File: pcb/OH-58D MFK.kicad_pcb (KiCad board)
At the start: 2 copper layers, 114.5 x 140 mm, 123 parts, among them J1 Conn_01x07_Pin, J2 Conn_01x10_Pin, J3 Conn_01x03_Pin, J4 Conn_01x02_Pin, J5 Conn_01x02_Pin, SW1 SW_Push, SW10 SW_Push, SW11 SW_Push, SW12 SW_Push, SW13 SW_Push, SW14 SW_Push, SW15 SW_Push, SW16 SW_Push, SW17 SW_Push, SW18 SW_Push, SW19 SW_Push, SW2 SW_Push, SW20 SW_Push, SW21 SW_Push, SW22 SW_Push, SW23 SW_Push, SW24 SW_Push, SW25 SW_Push, SW26 SW_Push, SW27 SW_Push, SW28 SW_Push, SW29 SW_Push, SW3 SW_Push, SW30 SW_Push, SW31 SW_Push, SW32 SW_Push, SW33 SW_Push, SW34 SW_Push, SW35 SW_Push, SW36 SW_Push, SW37 SW_Push, SW38 SW_Push, SW39 SW_Push, SW4 SW_Push, SW40 SW_Push, SW41 SW_Push, SW42 SW_Push, SW43 SW_Push, SW44 SW_Push, SW45 SW_Push, SW46 SW_Push, SW47 SW_Push, SW5 SW_Push, SW6 SW_Push, SW7 SW_Push, SW8 SW_Push, SW9 SW_Push

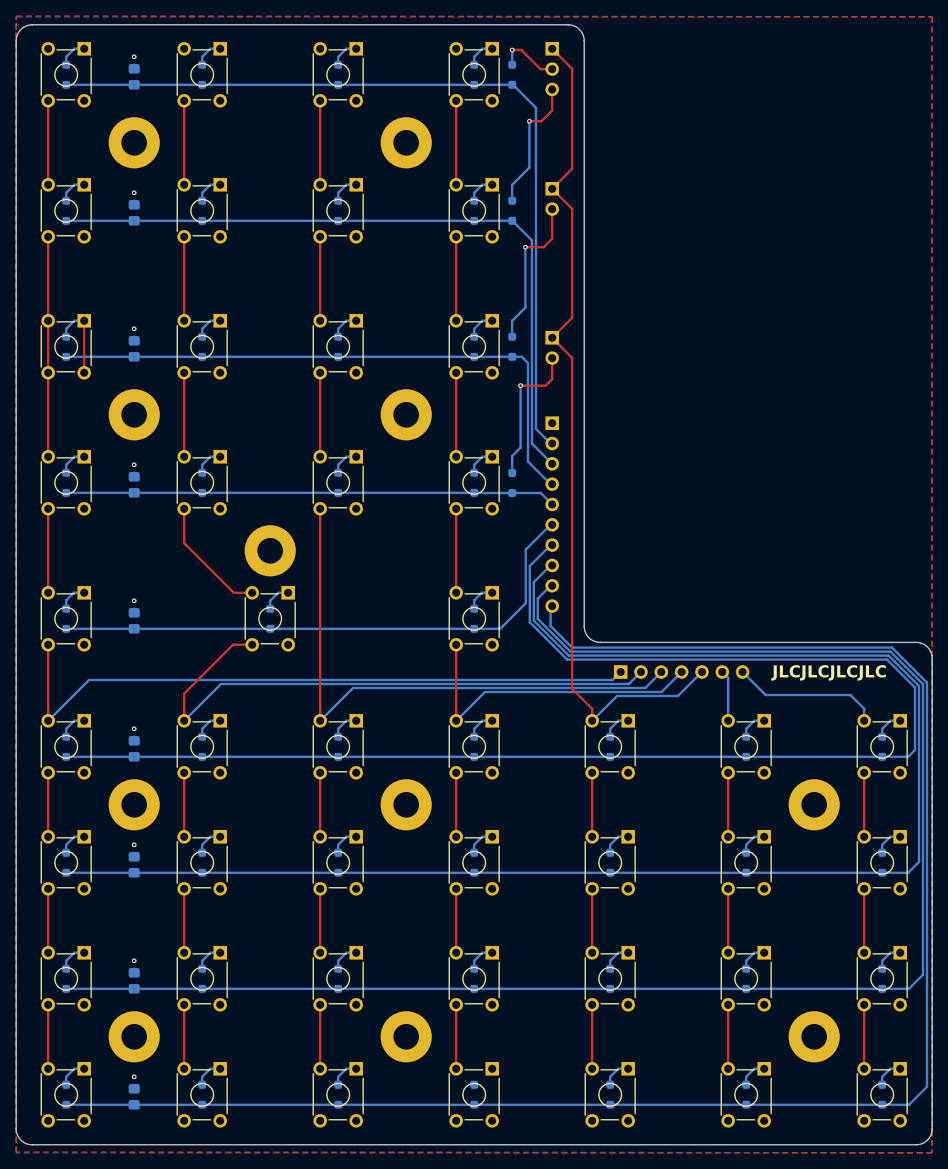
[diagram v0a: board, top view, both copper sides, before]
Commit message: Change package size for diodes
This commit also fixes silkscreen overlap warnings.
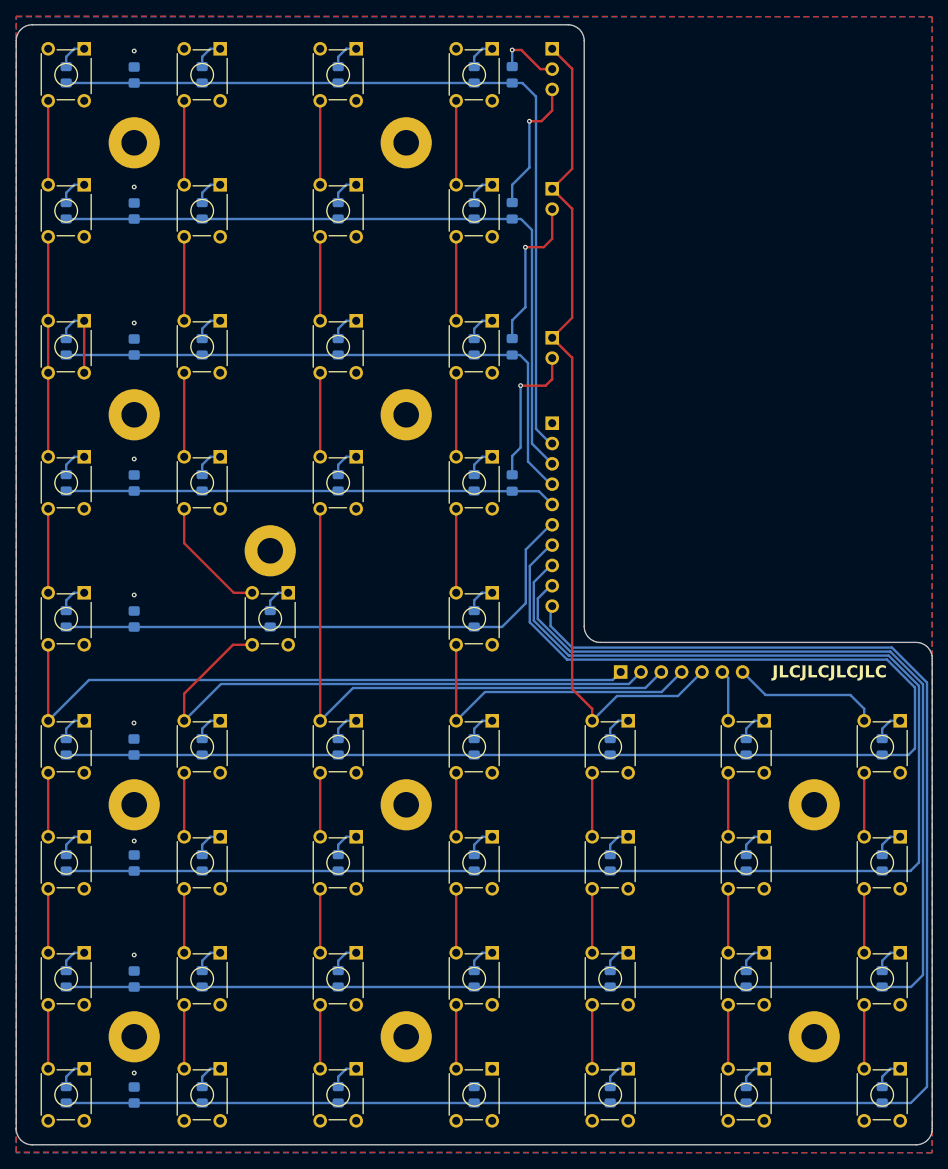
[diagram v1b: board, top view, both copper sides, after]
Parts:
- D1, D10, D11, D12, D13, D14, D15, D16, D17, D18, D19, D2, D20, D21, D22, D23, D24, D25, D26, D27, D28, D29, D3, D30, D31, D32, D33, D34, D35, D36, D37, D38, D39, D4, D40, D41, D42, D43, D44, D45, D46, D47, D48, D49, D5, D50, D51, D6, D7, D8, D9: footprint Diode_SMD:D_SOD-323_HandSoldering -> Diode_SMD:D_0805_2012Metric_Pad1.15x1.40mm_HandSolder
- moved R6 0.23 mm to (52.4, 125.0)
- moved R3 0.23 mm to (52.4, 75.0)
- moved R4 0.23 mm to (52.4, 92.0)
- moved R5 0.23 mm to (52.4, 109.0)
- moved R1 0.23 mm to (52.4, 41.0)
- moved R2 0.23 mm to (52.4, 58.0)
- moved R7 0.22 mm to (52.4, 139.6)
- moved R8 0.22 mm to (52.4, 154.1)
- moved R9 0.22 mm to (52.4, 168.6)
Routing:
- net Net-(D27-K): track 190.3 -> 189.1 mm
- net Net-(D20-K): track 178.0 -> 177.0 mm
- net Net-(D1-K): track 102.6 -> 103.6 mm
- net Net-(D41-K): track 213.1 -> 212.2 mm
- net Net-(D34-K): track 201.9 -> 201.0 mm
- net Net-(D49-K): track 88.4 -> 89.2 mm
